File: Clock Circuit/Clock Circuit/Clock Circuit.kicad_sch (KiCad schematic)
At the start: 24 parts, among them SW1 button, SW2 button, SW3 button, U1 74LS157, U1 LMC555xM, U2 LMC555xM

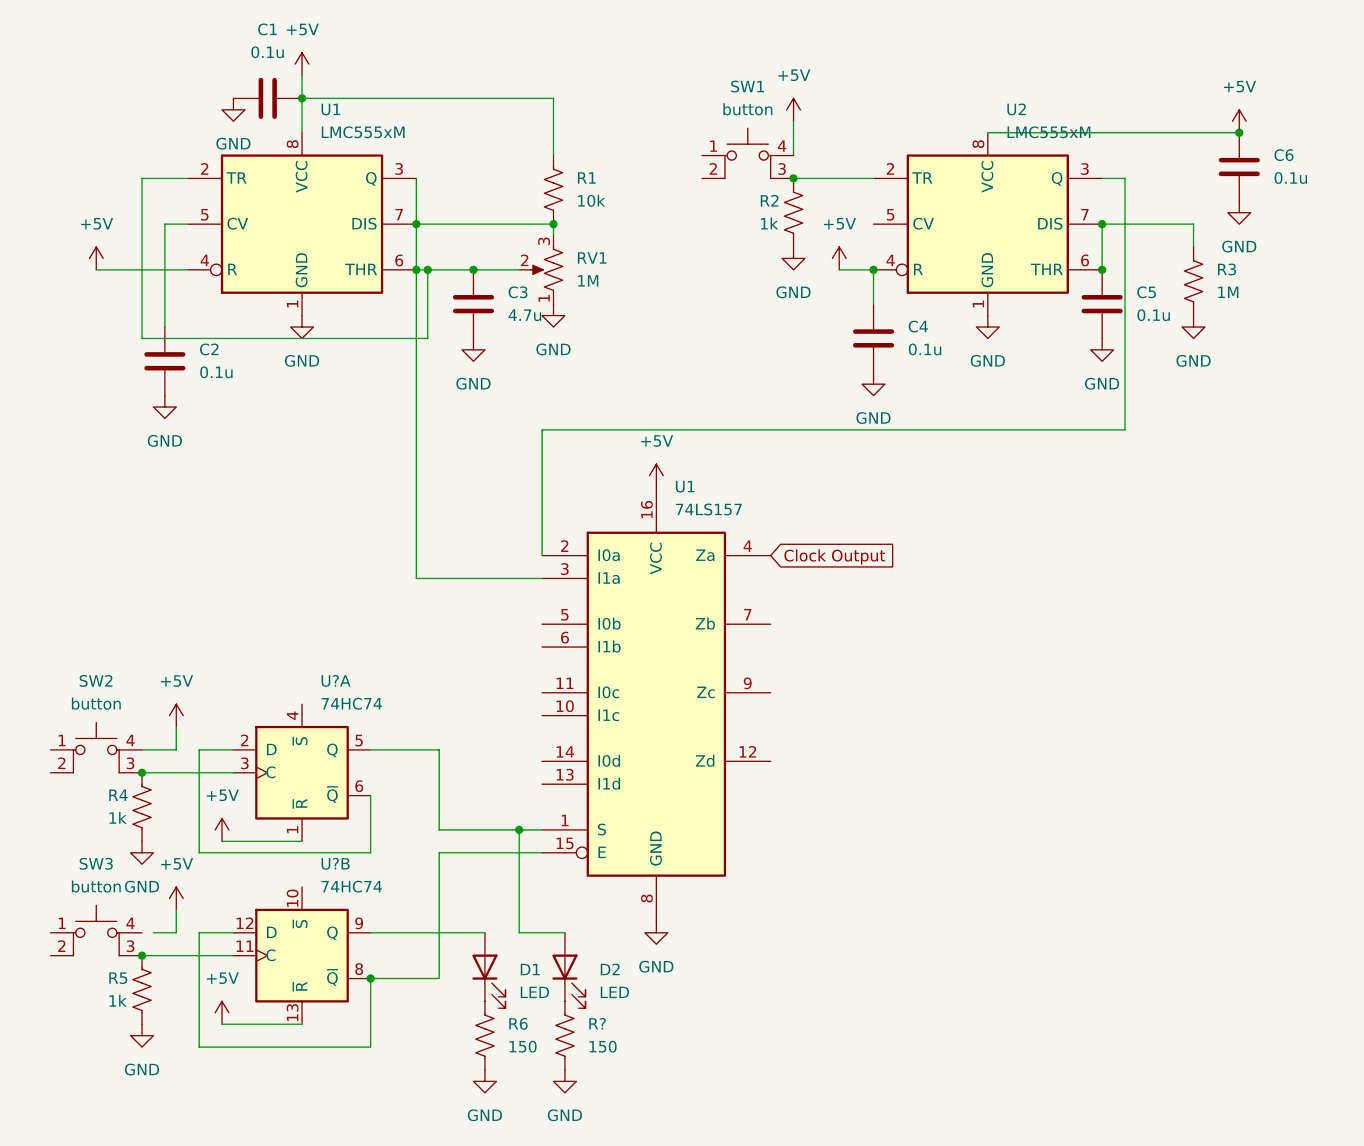
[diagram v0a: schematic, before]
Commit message: Updated clock circuits
Changed the design of the clock control circuit to use dip switches rather than the janky D flip flop or T flip flop. Also added a 1MHz clock.
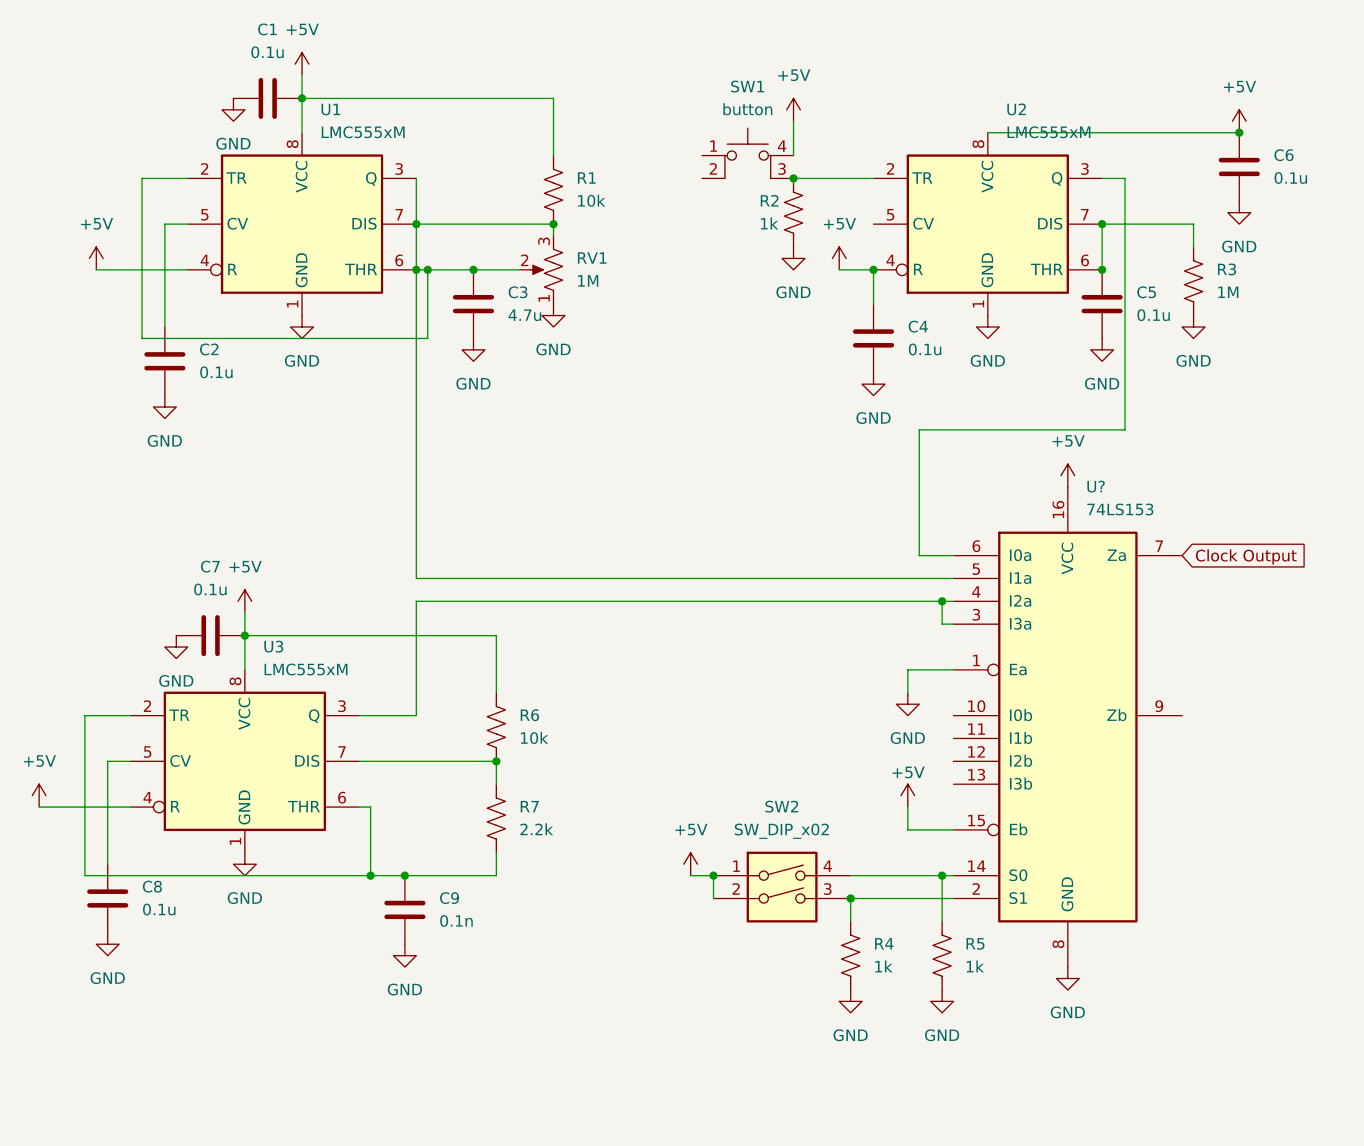
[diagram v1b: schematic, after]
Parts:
- removed D1, D2: LED, symbol Device:LED
- removed R?: 150, symbol Device:R_US
- removed SW2, SW3: button, symbol Switch:SW_MEC_5E
- removed U1: 74LS157, symbol 74xx:74LS157
- removed U? (x2): 74HC74, symbol 74xx:74HC74
- added C7, C8: 0.1u, symbol Device:C
- added C9: 0.1n, symbol Device:C
- added R7: 2.2k, symbol Device:R_US
- added SW2: SW_DIP_x02, symbol Switch:SW_DIP_x02
- added U3: LMC555xM, Package_SO:SOIC-8_3.9x4.9mm_P1.27mm, symbol Timer:LMC555xM
- added U?: 74LS153, symbol 74xx:74LS153
- R6: value 150 -> 10k
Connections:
- net +5V: now also R6.1, C7.2, SW2.1, SW2.2, U3.4 (R), U3.8 (VCC), U?.15 (Eb), U?.16 (VCC)
- net Clock Output: now also U?.7 (Za)
- net GND: now also C7.1, C8.2, C9.2, U3.1 (GND), U?.1 (Ea), U?.8 (GND); no longer R6.2
- net at R4.1: now also SW2.3, U?.2 (S1)
- net at R5.1: now also SW2.4, U?.14 (S0)
- net at C3.1, R1.2, RV1.2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: now also U?.5 (I1a)
- net at U2.3 (Q): now also U?.6 (I0a)
- new net: C9.1, R7.2, U3.2 (TR), U3.6 (THR)
- new net: U3.3 (Q), U?.3 (I3a), U?.4 (I2a)
- new net: R6.2, R7.1, U3.7 (DIS)
- new net: C8.1, U3.5 (CV)
